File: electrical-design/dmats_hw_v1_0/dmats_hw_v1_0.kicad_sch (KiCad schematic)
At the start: 23 parts, among them J1 Conn_01x06, J2 Conn_01x04, M1 Motor_DC, SW1 RotaryEncoder, U1 ABX00042, U2 L298N, U2 SENSE-ME, U3 L7805

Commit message: software tweaks and development of A4957 custom driver
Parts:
- removed U1: ABX00042, ABX00042:MODULE_ABX00042, symbol ABX00042:ABX00042
- removed U2: SENSE-ME, Connector_TE-Connectivity:TE_826576-6_1x06_P3.96mm_Vertical, symbol Connector_Generic:Conn_01x05
- added J3, J4: Hall_Effect_Sensor_Mod, symbol Connector:Conn_01x04_Pin
- added U1: ABX00042, ABX00042:MODULE_ABX00042, symbol ABX00042:ABX00042
- added U4: ~, symbol custom:NICLA_SENSE_ME
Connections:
- net +3.3V: now also U4.1 (3.3V)
- net +5V: now also J3.1 (Pin_1), J4.1 (Pin_1)
- net C1: now also U1.JA9 (D0)
- net C2: now also U1.JA10 (D1)
- net ENA: no longer U2.6 (EnA)
- net ENB: no longer U2.11 (EnB)
- net GND: now also J3.4 (Pin_4), J4.4 (Pin_4), U4.5 (GND)
- net GPIO_CS: now also U1.JD13 (D7), U4.4 (GOI_CS)
- net I2C-SCL: now also U1.JD8 (D12), U4.3 (I2C_SCL)
- net I2C-SDA: now also U1.JD9 (D11), U4.2 (I2C_SDA)
- net IN1: now also U1.JA11 (D2)
- net IN2: now also U1.JA12 (D3)
- net VIN: now also U1.JD2 (VIN_1)
- new net HES_A1: J3.3 (Pin_3), U1.JA2 (A0_D15)
- new net HES_A2: J4.3 (Pin_3), U1.JA3 (A1_D16)
- new net HES_D1: J3.2 (Pin_2), U1.JD14 (D6)
- new net HES_D2: J4.2 (Pin_2), U1.JA14 (D5)
- new net PWM_A: U1.JA13 (D4), U2.6 (EnA)
- new net PWM_B: U2.11 (EnB)

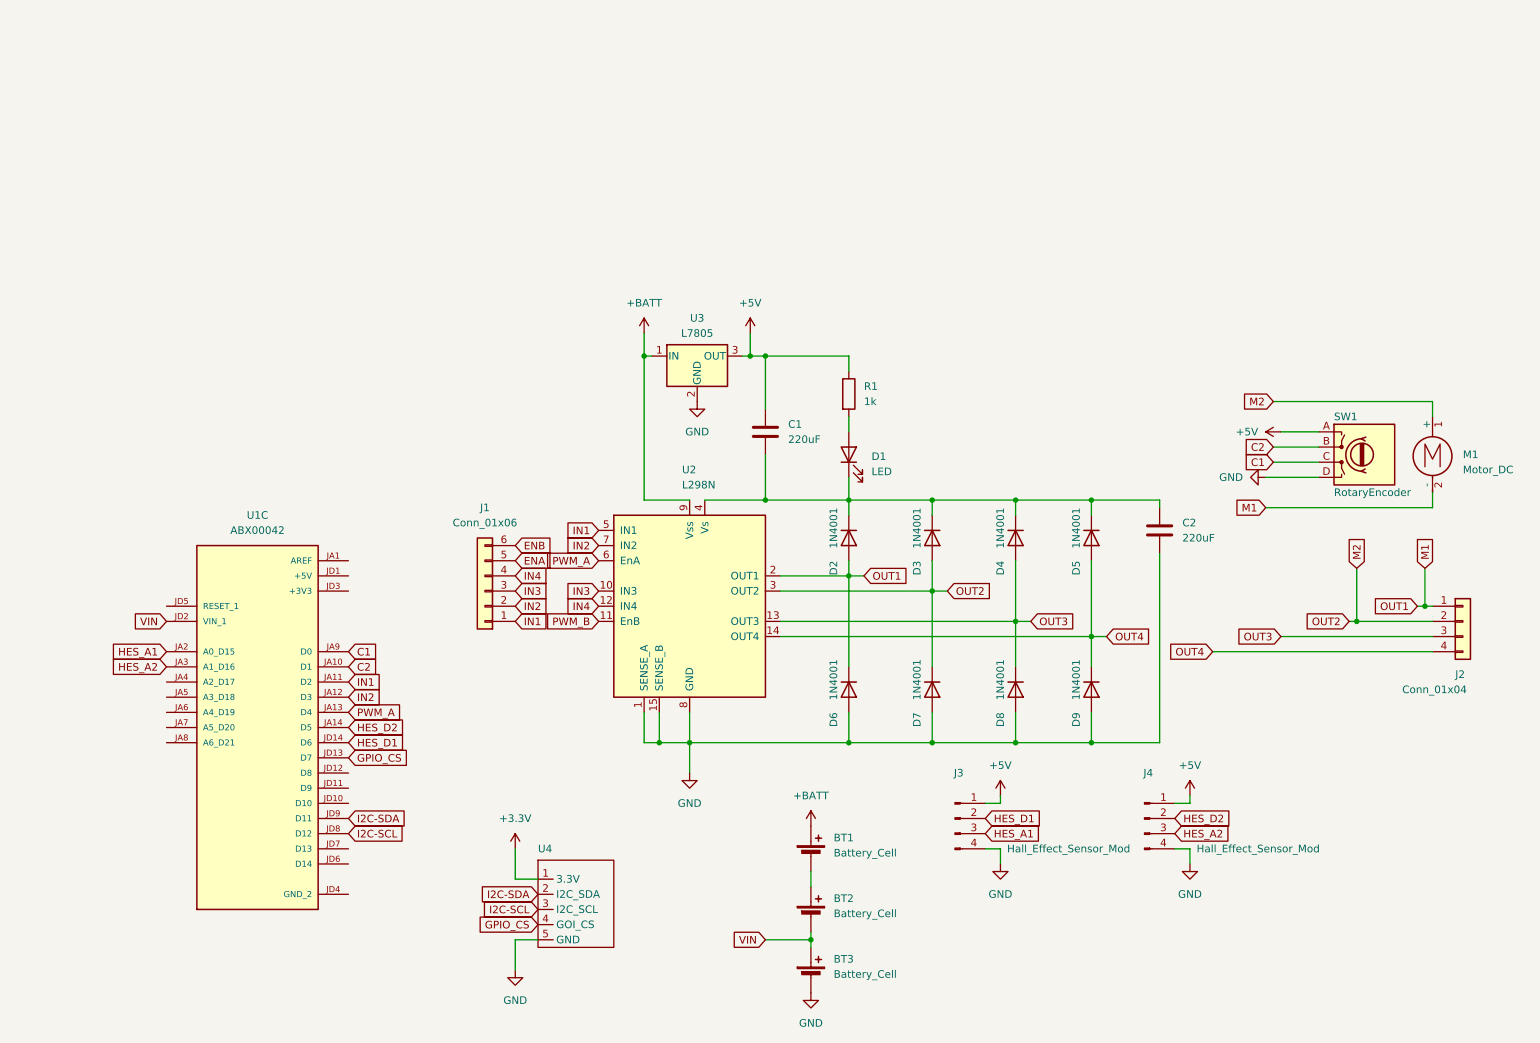
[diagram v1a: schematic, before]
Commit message: sim updates for force analysis and visual clean up on elec drawings
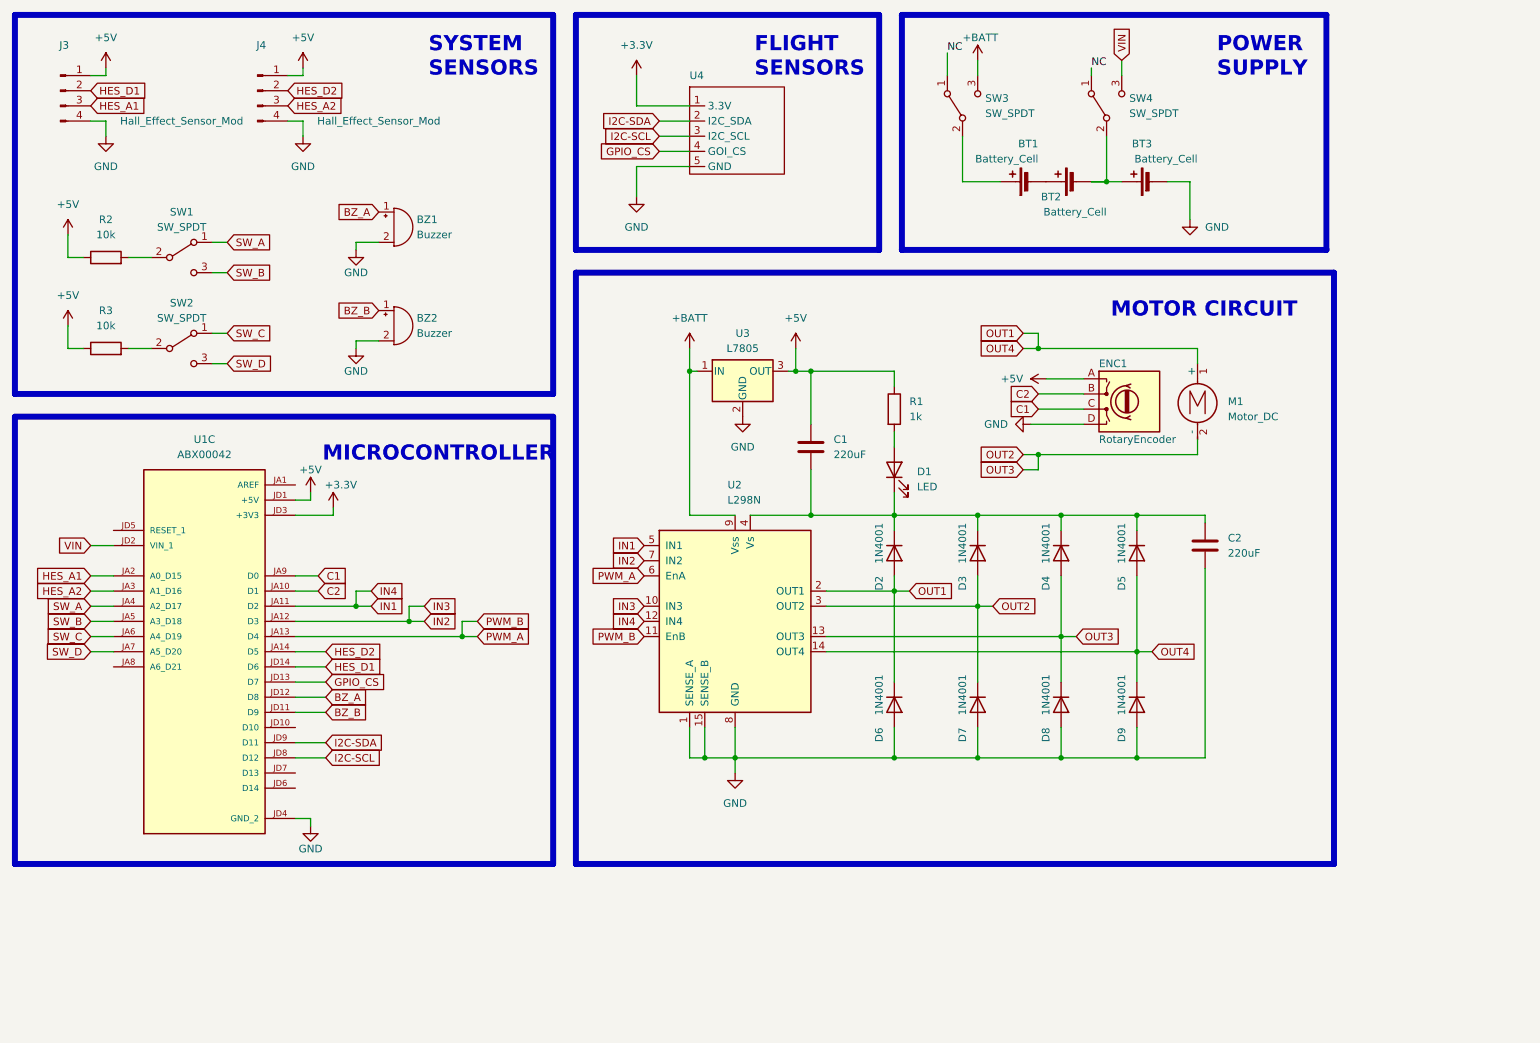
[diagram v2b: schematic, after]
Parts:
- removed J1: Conn_01x06, symbol Connector_Generic:Conn_01x06
- removed J2: Conn_01x04, symbol Connector_Generic:Conn_01x04
- added BZ1, BZ2: Buzzer, symbol Device:Buzzer
- added R2, R3: 10k, symbol Device:R
- added SW1, SW2, SW3, SW4: SW_SPDT, symbol Switch:SW_SPDT
- renumbered SW1 to ENC1
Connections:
- net IN3 is gone; now on net IN2: U2.10 (IN3)
- net IN4 is gone; now on net IN1: U2.12 (IN4)
- net OUT3 is gone; now on net OUT2: D4.2 (A), D8.1 (K), U2.13 (OUT3)
- net OUT4 is gone; now on net OUT1: D5.2 (A), D9.1 (K), U2.14 (OUT4)
- net PWM_B is gone; now on net PWM_A: U2.11 (EnB)
- net +3.3V: now also U1.JD3 (+3V3)
- net +5V: now also U1.JD1 (+5V), R2.1, R3.1
- net +BATT: now also SW3.3 (C); no longer BT1.1 (+)
- net GND: now also U1.JD4 (GND_2), BZ1.2 (+), BZ2.2 (+)
- net VIN: now also SW4.3 (C); no longer BT2.2 (-), BT3.1 (+)
- net SW_A: now reaches U1.JA4 (A2_D17)
- net SW_A: now also SW1.1 (A)
- net SW_B: now reaches U1.JA5 (A3_D18)
- net SW_B: now also SW1.3 (C)
- net SW_C: now reaches U1.JA6 (A4_D19)
- net SW_C: now also SW2.1 (A)
- net SW_D: now reaches U1.JA7 (A5_D20)
- net SW_D: now also SW2.3 (C)
- net BZ_B: now reaches U1.JD11 (D9)
- net BZ_B: now also BZ2.1 (-)
- net BZ_A: now reaches U1.JD12 (D8)
- net BZ_A: now also BZ1.1 (-)
- net M1 renamed OUT1
- net OUT1: now also M1.1 (+); no longer M1.2 (-)
- net M2 renamed OUT2
- net OUT2: now also M1.2 (-); no longer M1.1 (+)
- new net: R2.2, SW1.2 (B)
- new net: BT2.2 (-), BT3.1 (+), SW4.2 (B)
- new net: BT1.1 (+), SW3.2 (B)
- new net: R3.2, SW2.2 (B)
- new net NC: SW3.1 (A), SW4.1 (A)
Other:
- moved on the sheet: BT1, BT2, BT3, C1, C2, D1, D2, D3, D4, D5, D6, D7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
